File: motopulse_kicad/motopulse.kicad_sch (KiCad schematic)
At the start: 8 parts, among them J1 ESP32-S3_Left_Header, J2 ESP32-S3_Right_Header, J3 INMP441_Breakout, J4 OLED_0.96_I2C

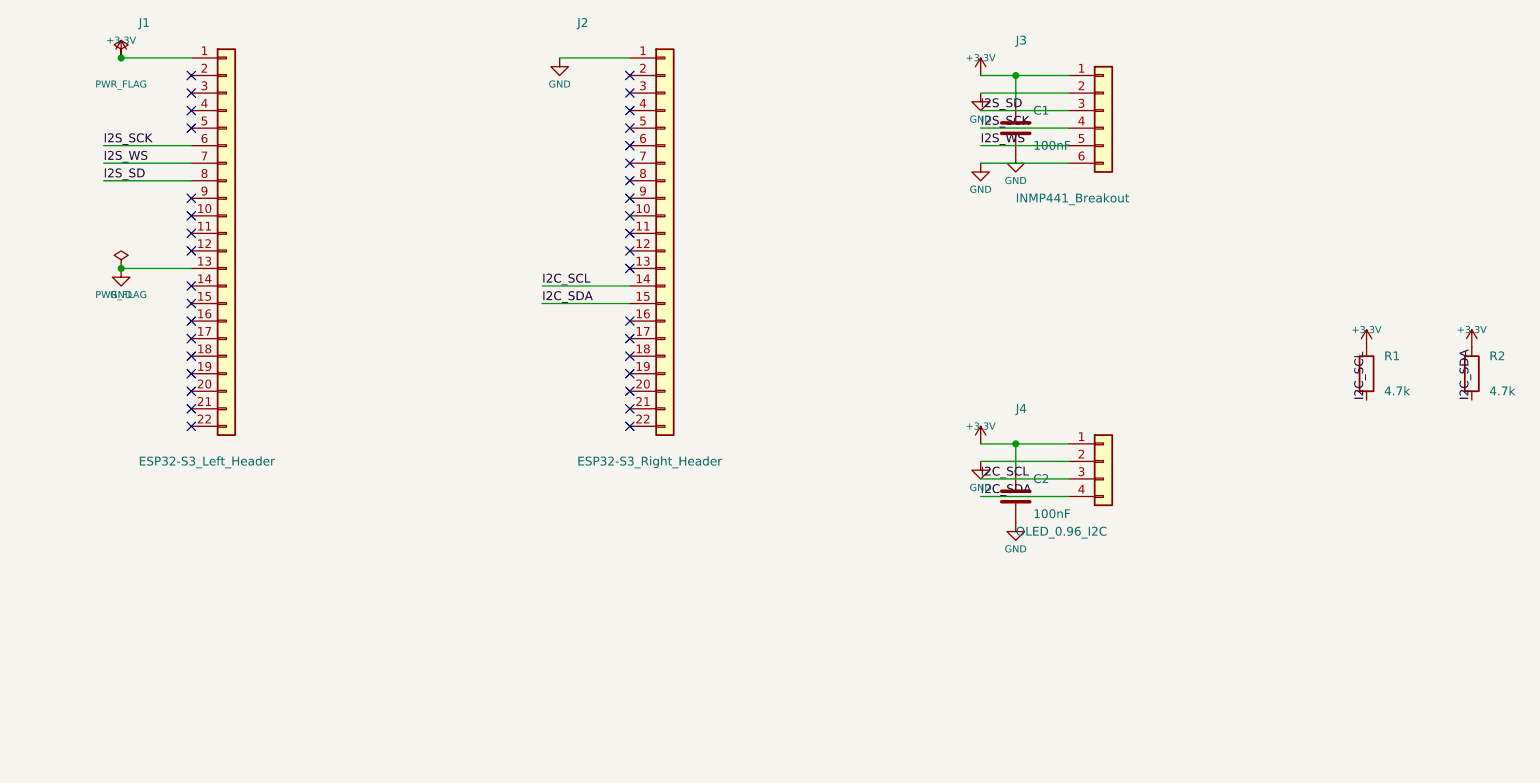
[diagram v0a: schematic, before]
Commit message: feat(hardware): unified ESP32-S3 carrier with 40mm dual mic, OLED, piezo and zero-capacitor layout
- ESP32-S3-DevKitC-1 (2x22 headers) unified motherboard
- Dual INMP441 MEMS microphones with exactly 40.0 mm baseline spacing
- 0.96 inch SSD1306 OLED display header
- Piezoelectric vibration sensor connector and 1M damping resistor
- Zero capacitors, pure direct-connect architecture
- KiCad ERC 0 errors, PCB DRC 0 violations, 0 unconnected items

Co-authored-by: ishannvn <ishannvn@users.noreply.github.com>
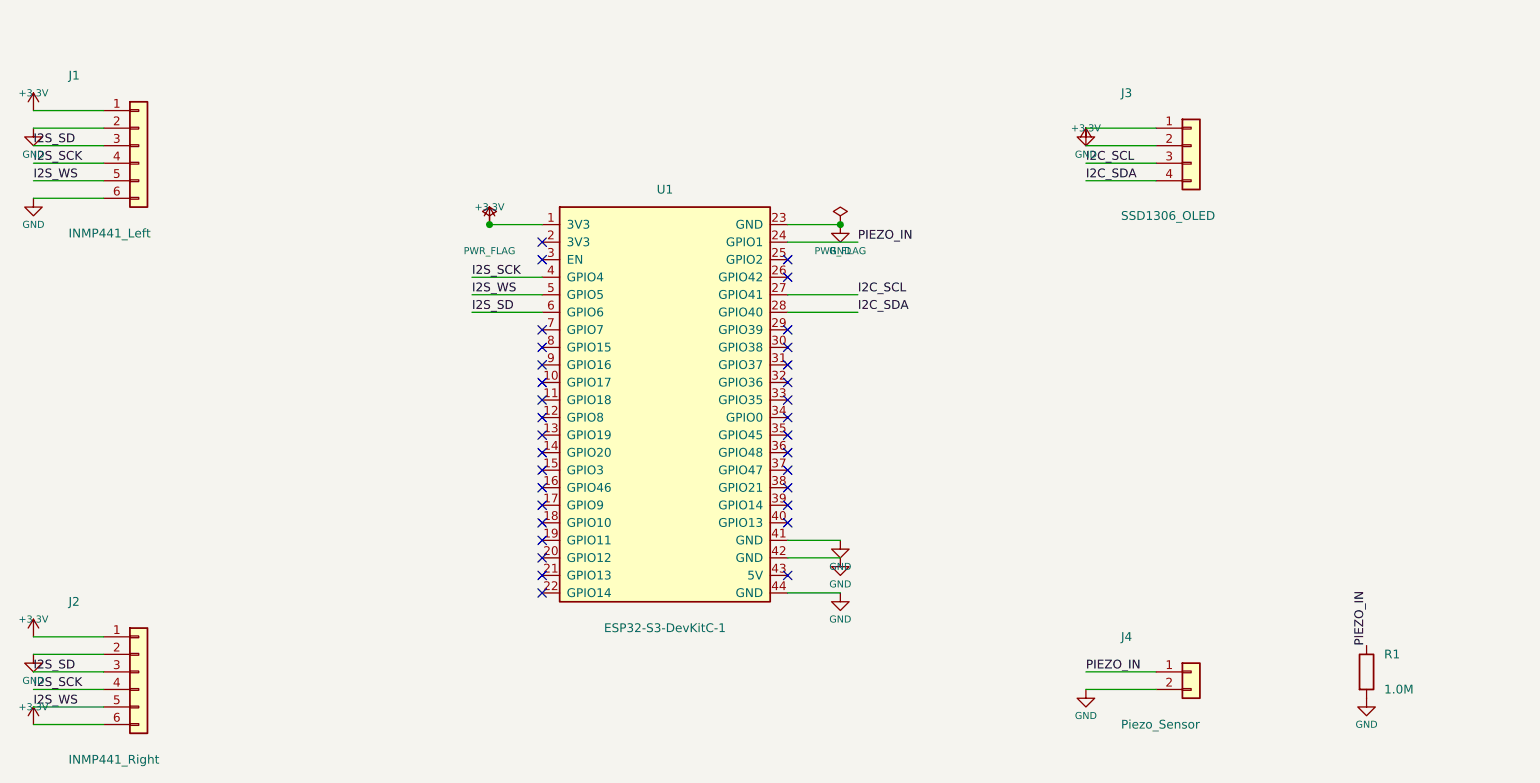
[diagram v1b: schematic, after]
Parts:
- removed C1, C2: 100nF, Capacitor_SMD:C_0805_2012Metric, symbol Device:C
- removed J1: ESP32-S3_Left_Header, Connector_PinHeader_2.54mm:PinHeader_1x22_P2.54mm_Vertical, symbol Connector_Generic:Conn_01x22
- removed J2: ESP32-S3_Right_Header, Connector_PinHeader_2.54mm:PinHeader_1x22_P2.54mm_Vertical, symbol Connector_Generic:Conn_01x22
- removed J3: INMP441_Breakout, Connector_PinHeader_2.54mm:PinHeader_1x06_P2.54mm_Vertical, symbol Connector_Generic:Conn_01x06
- removed J4: OLED_0.96_I2C, Connector_PinHeader_2.54mm:PinHeader_1x04_P2.54mm_Vertical, symbol Connector_Generic:Conn_01x04
- removed R2: 4.7k, Resistor_SMD:R_0805_2012Metric, symbol Device:R
- added J1: INMP441_Left, Connector_PinHeader_2.54mm:PinHeader_1x06_P2.54mm_Vertical, symbol Connector_Generic:Conn_01x06
- added J2: INMP441_Right, Connector_PinHeader_2.54mm:PinHeader_1x06_P2.54mm_Vertical, symbol Connector_Generic:Conn_01x06
- added J3: SSD1306_OLED, Connector_PinSocket_2.54mm:PinSocket_1x04_P2.54mm_Vertical, symbol Connector_Generic:Conn_01x04
- added J4: Piezo_Sensor, Connector_PinHeader_2.54mm:PinHeader_1x02_P2.54mm_Vertical, symbol Connector_Generic:Conn_01x02
- added U1: ESP32-S3-DevKitC-1, motopulse:ESP32-S3-DevKitC-1, symbol motopulse:ESP32-S3-DevKitC-1
- R1: value 4.7k -> 1.0M
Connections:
- net +3.3V: now also J1.1 (Pin_1), J2.1 (Pin_1), J2.6 (Pin_6), J3.2 (Pin_2), U1.1 (3V3); no longer R1.1
- net GND: now also R1.2, J1.2 (Pin_2), J1.6 (Pin_6), J2.2 (Pin_2), J3.1 (Pin_1), J4.2 (Pin_2), U1.23 (GND), U1.41 (GND), U1.42 (GND), U1.44 (GND)
- net I2C_SCL: now also J3.3 (Pin_3), U1.27 (GPIO41); no longer R1.2
- net I2C_SDA: now also J3.4 (Pin_4), U1.28 (GPIO40)
- net I2S_SCK: now also J1.4 (Pin_4), J2.4 (Pin_4), U1.4 (GPIO4)
- net I2S_SD: now also J1.3 (Pin_3), J2.3 (Pin_3), U1.6 (GPIO6)
- net I2S_WS: now also J1.5 (Pin_5), J2.5 (Pin_5), U1.5 (GPIO5)
- new net PIEZO_IN: J4.1 (Pin_1), R1.1, U1.24 (GPIO1)
- no-connect marks 36 -> 33
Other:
- company: IEEE RUAS - Hacktivate 2026 -> MotoPulse Team
- title: MotoPulse: Automotive Acoustic Predictive Maintenance -> MotoPulse Unified ESP32-S3 Acoustic & Vibration Motherboard

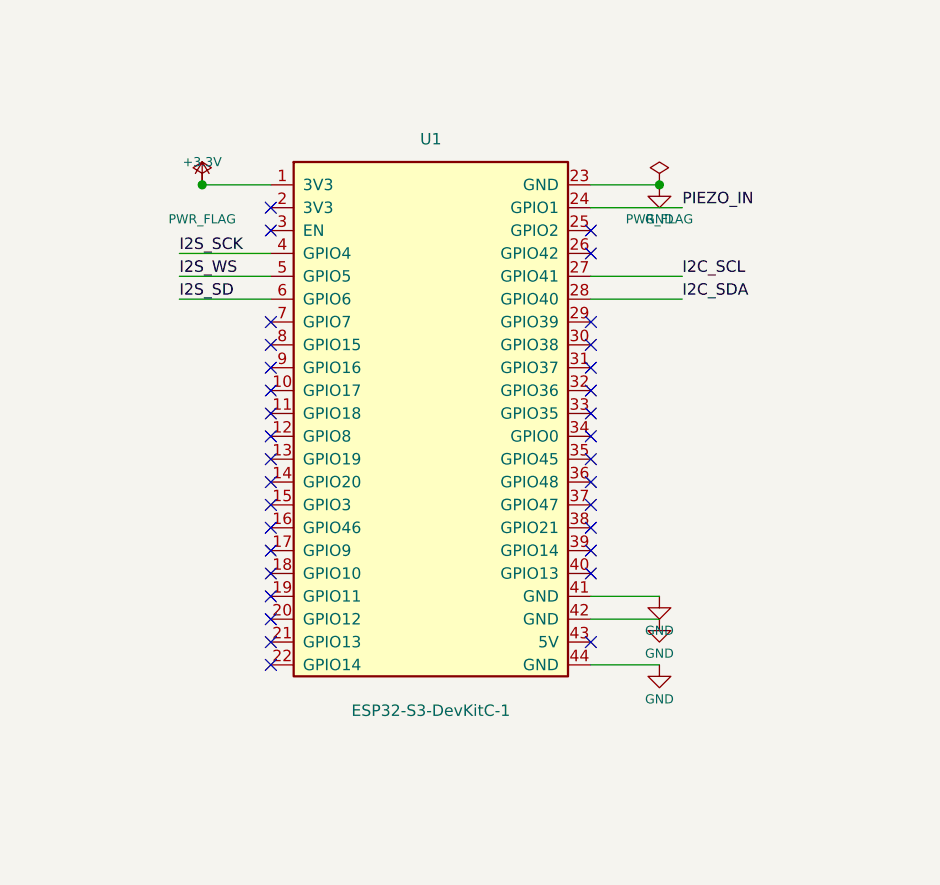
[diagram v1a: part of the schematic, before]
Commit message: fix(hardware): update KiCad schematic and PCB to match ESP32-S3-DevKitC-1-N16R8 pinout
- Updated 44-pin schematic symbol to official ESP32-S3-DevKitC-1-N16R8 pin layout
- Corrected J1 header pins (1-22) with 3V3, RST, GPIO4-6, GPIO7-21, GND
- Corrected J3 header pins (23-44) with 3V3, 5V, GND, GPIO1 (Piezo), GPIO41/40 (I2C OLED), Octal PSRAM reservation (GPIO35-37), GND
- Updated silkscreen labels and board footprint to ESP32-S3-WROOM-1 N16R8
- Verified 0 ERC violations and 0 PCB DRC violations (0 unconnected items)

Co-authored-by: ishannvn <ishannvn@users.noreply.github.com>
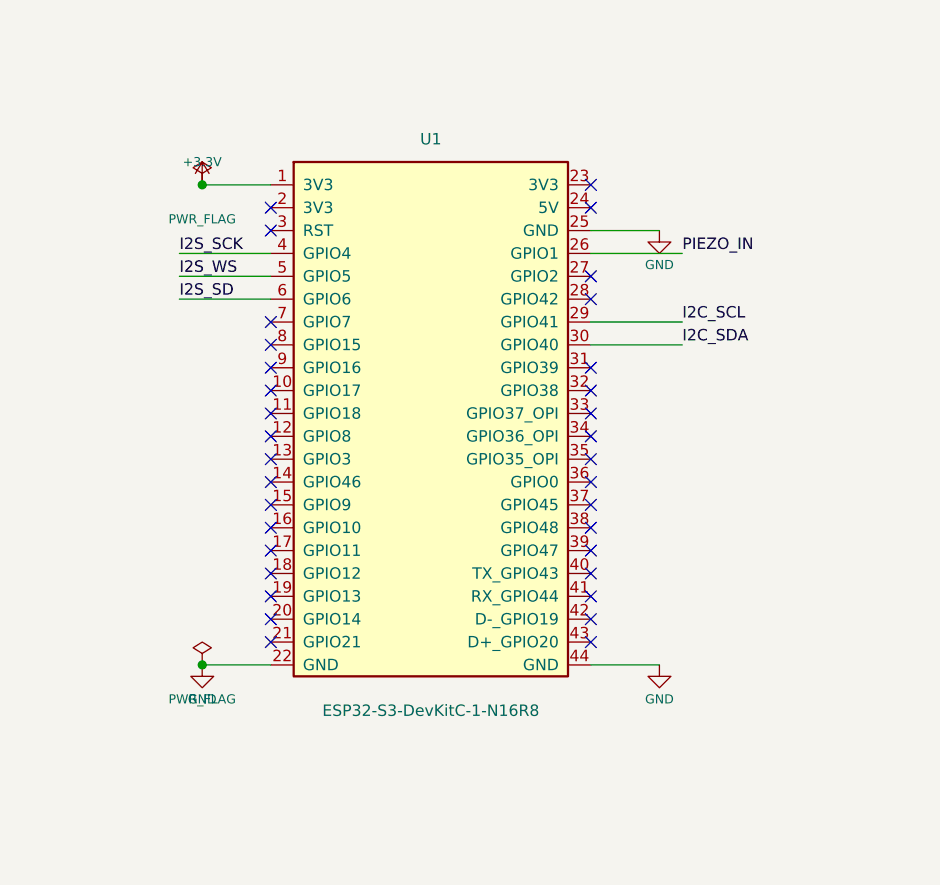
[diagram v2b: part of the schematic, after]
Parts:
- removed U1: ESP32-S3-DevKitC-1, motopulse:ESP32-S3-DevKitC-1, symbol motopulse:ESP32-S3-DevKitC-1
- added U1: ESP32-S3-DevKitC-1-N16R8, motopulse:ESP32-S3-DevKitC-1, symbol motopulse:ESP32-S3-DevKitC-1-N16R8
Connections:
- net +3.3V: now also U1.1 (3V3)
- net GND: now also U1.22 (GND), U1.25 (GND), U1.44 (GND)
- net I2C_SCL: now also U1.29 (GPIO41)
- net I2C_SDA: now also U1.30 (GPIO40)
- net I2S_SCK: now also U1.4 (GPIO4)
- net I2S_SD: now also U1.6 (GPIO6)
- net I2S_WS: now also U1.5 (GPIO5)
- net PIEZO_IN: now also U1.26 (GPIO1)
- no-connect marks 33 -> 34
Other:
- title: MotoPulse Unified ESP32-S3 Acoustic & Vibration Motherboard -> MotoPulse ESP32-S3-DevKitC-1-N16R8 Acoustic & Vibration Carrier

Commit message: fix(hardware): route OLED I2C SCL to GPIO 8 and SDA to GPIO 9
- Reconnected 0.96 inch SSD1306 OLED I2C lines:
  - SCL -> GPIO 8 (Pin 12 on ESP32-S3-DevKitC-1-N16R8)
  - SDA -> GPIO 9 (Pin 15 on ESP32-S3-DevKitC-1-N16R8)
- Updated PCB router with layer-separated orthogonal paths around U1
- Verified 0 ERC violations and 0 PCB DRC violations with 0 unconnected items

Co-authored-by: ishannvn <ishannvn@users.noreply.github.com>
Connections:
- net I2C_SCL: now also U1.12 (GPIO8); no longer U1.29 (GPIO41)
- net I2C_SDA: now also U1.15 (GPIO9); no longer U1.30 (GPIO40)
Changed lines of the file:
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@@
+	(wire
+		(pts
+			(xy 121.92 115.57)
+			(xy 111.76 115.57)
+		)
+		(stroke (width 0) (type default))
+	)
+	(wire
+		(pts
+			(xy 121.92 123.19)
+			(xy 111.76 123.19)
+		)
+		(stroke (width 0) (type default))
+	)
 	(wire
 		(pts
@@
 	(wire
 		(pts
-			(xy 157.48 102.87)
-			(xy 167.64 102.87)
-		)
-		(stroke (width 0) (type default))
-	)
-	(wire
-		(pts
-			(xy 157.48 105.41)
-			(xy 167.64 105.41)
-		)
-		(stroke (width 0) (type default))
-	)
-	(wire
-		(pts
 			(xy 157.48 140.97)
 			(xy 165.10 140.97)
@@
 		)
 	)
+	(label "I2C_SCL"
+		(at 111.76 115.57 180)
+		(fields_autoplaced yes)
+		(effects
+			(font (size 1.27 1.27))
+			(justify left bottom)
+		)
+	)
+	(label "I2C_SDA"
+		(at 111.76 123.19 180)
+		(fields_autoplaced yes)
+		(effects
+			(font (size 1.27 1.27))
+			(justify left bottom)
+		)
+	)
 	(label "PIEZO_IN"
 		(at 167.64 95.25 0)
@@
 		)
 	)
-	(label "I2C_SCL"
-		(at 167.64 102.87 0)
-		(fields_autoplaced yes)
-		(effects
-			(font (size 1.27 1.27))
-			(justify left bottom)
-		)
-	)
-	(label "I2C_SDA"
-		(at 167.64 105.41 0)
-		(fields_autoplaced yes)
-		(effects
-			(font (size 1.27 1.27))
-			(justify left bottom)
-		)
-	)
 	(label "I2S_SD"
 		(at 48.26 76.20 180)
@@
 	)
 	(no_connect
-		(at 121.92 115.57)
-	)
-	(no_connect
 		(at 121.92 118.11)
 	)
@@
 	)
 	(no_connect
-		(at 121.92 123.19)
-	)
-	(no_connect
 		(at 121.92 125.73)
 	)
@@
 	(no_connect
 		(at 157.48 100.33)
+	)
+	(no_connect
+		(at 157.48 102.87)
+	)
+	(no_connect
+		(at 157.48 105.41)
 	)
 	(no_connect
@@
 		(instances
 			(project "motopulse"
-				(path "/01a361da-1e3a-4de2-bc4b-16a0dab44124"
+				(path "/c76b0f79-a86d-419f-9d36-3083a6c1a626"
 					(reference "U1")
 					(unit 1)
@@
 		(instances
 			(project "motopulse"
-				(path "/01a361da-1e3a-4de2-bc4b-16a0dab44124"
+				(path "/c76b0f79-a86d-419f-9d36-3083a6c1a626"
 					(reference "#PWR01")
 					(unit 1)
@@
 		(instances
 			(project "motopulse"
-				(path "/01a361da-1e3a-4de2-bc4b-16a0dab44124"
+				(path "/c76b0f79-a86d-419f-9d36-3083a6c1a626"
 					(reference "#FLG01")
 					(unit 1)
@@
 		(instances
 			(project "motopulse"
-				(path "/01a361da-1e3a-4de2-bc4b-16a0dab44124"
+				(path "/c76b0f79-a86d-419f-9d36-3083a6c1a626"
 					(reference "#PWR02")
 					(unit 1)
@@
 		(instances
 			(project "motopulse"
-				(path "/01a361da-1e3a-4de2-bc4b-16a0dab44124"
+				(path "/c76b0f79-a86d-419f-9d36-3083a6c1a626"
 					(reference "#FLG02")
 					(unit 1)
@@
 		(instances
 			(project "motopulse"
-				(path "/01a361da-1e3a-4de2-bc4b-16a0dab44124"
+				(path "/c76b0f79-a86d-419f-9d36-3083a6c1a626"
 					(reference "#PWR03")
 					(unit 1)
@@
 		(instances
 			(project "motopulse"
-				(path "/01a361da-1e3a-4de2-bc4b-16a0dab44124"
+				(path "/c76b0f79-a86d-419f-9d36-3083a6c1a626"
 					(reference "#PWR04")
 					(unit 1)
@@
 		(instances
 			(project "motopulse"
-				(path "/01a361da-1e3a-4de2-bc4b-16a0dab44124"
+				(path "/c76b0f79-a86d-419f-9d36-3083a6c1a626"
 					(reference "J1")
 					(unit 1)
@@
 		(instances
 			(project "motopulse"
-				(path "/01a361da-1e3a-4de2-bc4b-16a0dab44124"
+				(path "/c76b0f79-a86d-419f-9d36-3083a6c1a626"
 					(reference "#PWR05")
 					(unit 1)
@@
 		(instances
 			(project "motopulse"
-				(path "/01a361da-1e3a-4de2-bc4b-16a0dab44124"
+				(path "/c76b0f79-a86d-419f-9d36-3083a6c1a626"
 					(reference "#PWR06")
 					(unit 1)
@@
 		(instances
 			(project "motopulse"
-				(path "/01a361da-1e3a-4de2-bc4b-16a0dab44124"
+				(path "/c76b0f79-a86d-419f-9d36-3083a6c1a626"
 					(reference "#PWR07")
 					(unit 1)
@@
 		(instances
 			(project "motopulse"
-				(path "/01a361da-1e3a-4de2-bc4b-16a0dab44124"
+				(path "/c76b0f79-a86d-419f-9d36-3083a6c1a626"
 					(reference "J2")
 					(unit 1)
@@
 		(instances
 			(project "motopulse"
-				(path "/01a361da-1e3a-4de2-bc4b-16a0dab44124"
+				(path "/c76b0f79-a86d-419f-9d36-3083a6c1a626"
 					(reference "#PWR08")
 					(unit 1)
@@
 		(instances
 			(project "motopulse"
-				(path "/01a361da-1e3a-4de2-bc4b-16a0dab44124"
+				(path "/c76b0f79-a86d-419f-9d36-3083a6c1a626"
 					(reference "#PWR09")
 					(unit 1)
@@
 		(instances
 			(project "motopulse"
-				(path "/01a361da-1e3a-4de2-bc4b-16a0dab44124"
+				(path "/c76b0f79-a86d-419f-9d36-3083a6c1a626"
 					(reference "#PWR10")
 					(unit 1)
@@
 		(instances
 			(project "motopulse"
-				(path "/01a361da-1e3a-4de2-bc4b-16a0dab44124"
+				(path "/c76b0f79-a86d-419f-9d36-3083a6c1a626"
 					(reference "J3")
 					(unit 1)
@@
 		(instances
 			(project "motopulse"
-				(path "/01a361da-1e3a-4de2-bc4b-16a0dab44124"
+				(path "/c76b0f79-a86d-419f-9d36-3083a6c1a626"
 					(reference "#PWR11")
 					(unit 1)
@@
 		(instances
 			(project "motopulse"
-				(path "/01a361da-1e3a-4de2-bc4b-16a0dab44124"
+				(path "/c76b0f79-a86d-419f-9d36-3083a6c1a626"
 					(reference "#PWR12")
 					(unit 1)
@@
 		(instances
 			(project "motopulse"
-				(path "/01a361da-1e3a-4de2-bc4b-16a0dab44124"
+				(path "/c76b0f79-a86d-419f-9d36-3083a6c1a626"
 					(reference "J4")
 					(unit 1)
@@
 		(instances
 			(project "motopulse"
-				(path "/01a361da-1e3a-4de2-bc4b-16a0dab44124"
+				(path "/c76b0f79-a86d-419f-9d36-3083a6c1a626"
 					(reference "#PWR13")
 					(unit 1)
@@
 		(instances
 			(project "motopulse"
-				(path "/01a361da-1e3a-4de2-bc4b-16a0dab44124"
+				(path "/c76b0f79-a86d-419f-9d36-3083a6c1a626"
 					(reference "R1")
 					(unit 1)
@@
 		(instances
 			(project "motopulse"
-				(path "/01a361da-1e3a-4de2-bc4b-16a0dab44124"
+				(path "/c76b0f79-a86d-419f-9d36-3083a6c1a626"
 					(reference "#PWR14")
 					(unit 1)
